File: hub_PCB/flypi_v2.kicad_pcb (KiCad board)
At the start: 2 copper layers, 76 x 85 mm, 35 parts, among them CON1 BARREL JACK, J12 USB A, P1 D1, P10 A2, P11 A3, P12 I2C 1, P13 I2C 2, P14 12V, P15 UART, P2 D2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

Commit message: Update flypi_v2.kicad_pcb
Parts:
- renumbered J12 to J1
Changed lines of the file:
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@@
     (descr "USB A vertical female connector, right angle")
     (tags "USB_A_Vertical female connector angled 73725-0110BLF")
-    (fp_text reference J12 (at 3 8.5 90) (layer F.SilkS)
+    (fp_text reference J1 (at 3 8.5 90) (layer F.SilkS)
       (effects (font (size 1 1) (thickness 0.15)))
     )

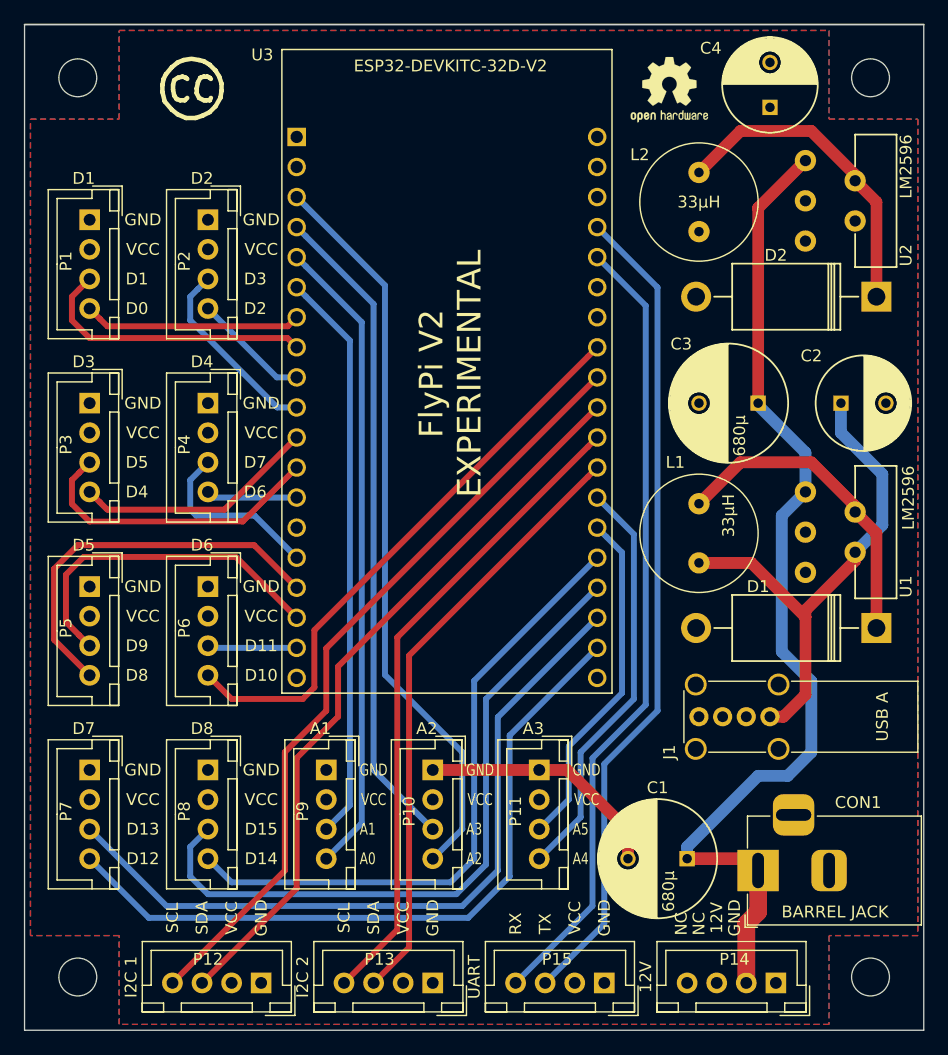
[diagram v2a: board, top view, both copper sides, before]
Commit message: Changed pinout to VCC-GND
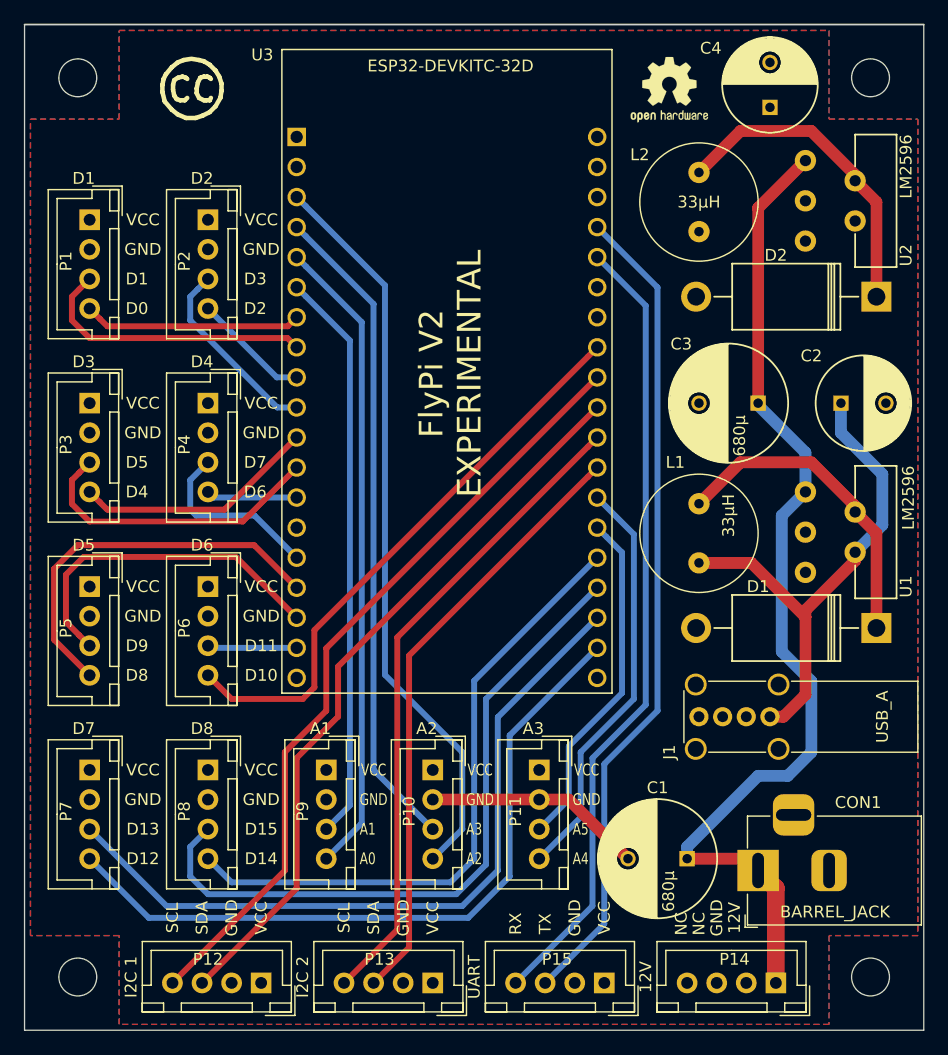
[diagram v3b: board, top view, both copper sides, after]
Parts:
- CON1: value BARREL JACK -> BARREL_JACK
- J1: value USB A -> USB_A
- U3: value ESP32-DEVKITC-32D-V2 -> ESP32-DEVKITC-32D
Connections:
- P1 pad 1: GND -> +5V
- P1 pad 2: +5V -> GND
- P10 pad 1: GND -> +5V
- P10 pad 2: +5V -> GND
- P11 pad 1: GND -> +5V
- P11 pad 2: +5V -> GND
- P12 pad 1: GND -> +5V
- P12 pad 2: +5V -> GND
- P13 pad 1: GND -> +5V
- P13 pad 2: +5V -> GND
- P14 pad 1: GND -> Net-(C1-Pad1)
- P14 pad 2: Net-(C1-Pad1) -> GND
- P15 pad 1: GND -> +5V
- P15 pad 2: +5V -> GND
- P2 pad 1: GND -> +5V
- P2 pad 2: +5V -> GND
- P3 pad 1: GND -> +5V
- P3 pad 2: +5V -> GND
- P4 pad 1: GND -> +5V
- P4 pad 2: +5V -> GND
- P5 pad 1: GND -> +5V
- P5 pad 2: +5V -> GND
- P6 pad 1: GND -> +5V
- P6 pad 2: +5V -> GND
- P7 pad 1: GND -> +5V
- P7 pad 2: +5V -> GND
- P8 pad 1: GND -> +5V
- P8 pad 2: +5V -> GND
- P9 pad 1: GND -> +5V
- P9 pad 2: +5V -> GND
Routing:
- net Net-(C1-Pad1): track 99.9 -> 86.5 mm
- net GND: track 21.0 -> 18.6 mm
